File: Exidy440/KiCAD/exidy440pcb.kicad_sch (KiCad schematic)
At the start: 0 parts

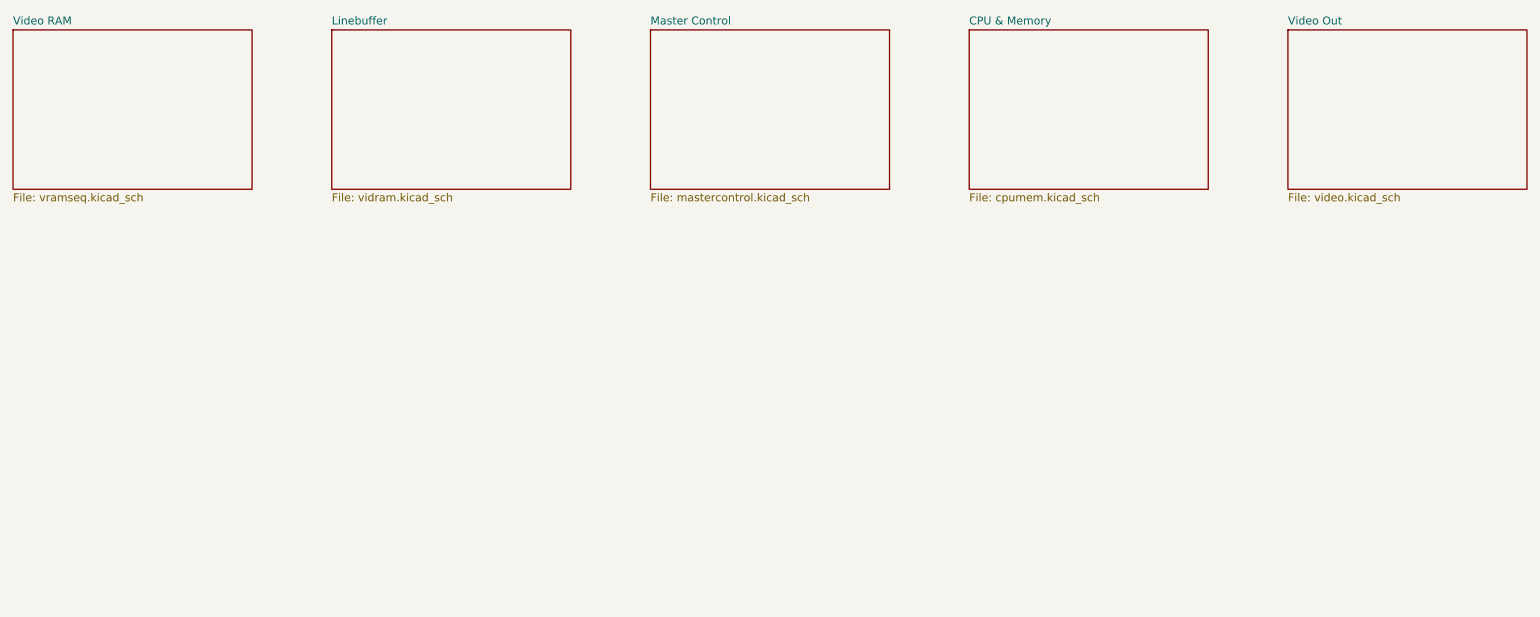
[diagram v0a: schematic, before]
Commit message: Added dual PCB structure, misc fixes and start of audio board IO
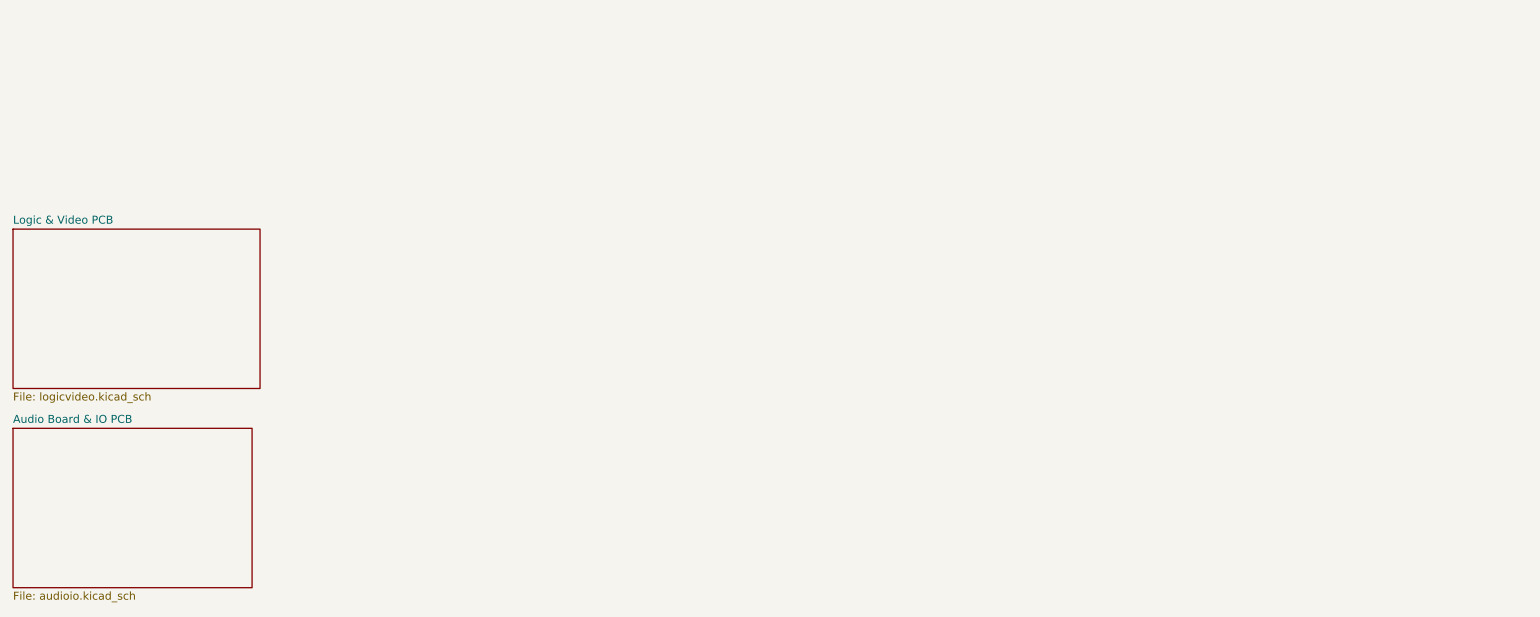
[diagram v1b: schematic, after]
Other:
- removed sheet CPU & Memory
- removed sheet Linebuffer
- removed sheet Master Control
- removed sheet Video Out
- removed sheet Video RAM
- added sheet Audio Board & IO PCB (audioio.kicad_sch)
- added sheet Logic & Video PCB (logicvideo.kicad_sch)
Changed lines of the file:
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@@
 	)
 	(sheet
-		(at 127 25.4)
+		(at 25.4 88.9)
 		(size 38.1 25.4)
 		(fields_autoplaced yes)
@@
 			(color 0 0 0 0.0000)
 		)
-		(property "Sheetname" "Master Control"
-			(at 127 24.6884 0)
+		(property "Sheetname" "Audio Board & IO PCB"
+			(at 25.4 88.1884 0)
 			(effects
 				(font
@@
 			)
 		)
-		(property "Sheetfile" "mastercontrol.kicad_sch"
-			(at 127 51.3846 0)
+		(property "Sheetfile" "audioio.kicad_sch"
+			(at 25.4 114.8846 0)
 			(effects
 				(font
@@
 			(project "exidy440pcb"
 				(path "/ee9ca5df-edb9-4677-bdcd-afd3abb310eb"
-					(page "3")
+					(page "AIDX")
 				)
 			)
@@
 	)
 	(sheet
-		(at 76.2 25.4)
-		(size 38.1 25.4)
+		(at 25.4 57.15)
+		(size 39.37 25.4)
 		(fields_autoplaced yes)
 		(stroke
@@
 			(color 0 0 0 0.0000)
 		)
-		(property "Sheetname" "Linebuffer"
-			(at 76.2 24.6884 0)
+		(property "Sheetname" "Logic & Video PCB"
+			(at 25.4 56.4384 0)
 			(effects
 				(font
@@
 			)
 		)
-		(property "Sheetfile" "vidram.kicad_sch"
-			(at 76.2 51.3846 0)
+		(property "Sheetfile" "logicvideo.kicad_sch"
+			(at 25.4 83.1346 0)
 			(effects
 				(font
@@
 			(project "exidy440pcb"
 				(path "/ee9ca5df-edb9-4677-bdcd-afd3abb310eb"
-					(page "2")
-				)
-			)
-		)
-	)
-	(sheet
-		(at 228.6 25.4)
-		(size 38.1 25.4)
-		(fields_autoplaced yes)
-		(stroke
-			(width 0.1524)
-			(type solid)
-		)
-		(fill
-			(color 0 0 0 0.0000)
-		)
-		(property "Sheetname" "Video Out"
-			(at 228.6 24.6884 0)
-			(effects
-				(font
-					(size 1.27 1.27)
-				)
-				(justify left bottom)
-			)
-		)
-		(property "Sheetfile" "video.kicad_sch"
-			(at 228.6 51.3846 0)
-			(effects
-				(font
-					(size 1.27 1.27)
-				)
-				(justify left top)
-			)
-		)
-		(instances
-			(project "exidy440pcb"
-				(path "/ee9ca5df-edb9-4677-bdcd-afd3abb310eb"
-					(page "5")
-				)
-			)
-		)
-	)
-	(sheet
-		(at 25.4 25.4)
-		(size 38.1 25.4)
-		(fields_autoplaced yes)
-		(stroke
-			(width 0.1524)
-			(type solid)
-		)
-		(fill
-			(color 0 0 0 0.0000)
-		)
-		(property "Sheetname" "Video RAM"
-			(at 25.4 24.6884 0)
-			(effects
-				(font
-					(size 1.27 1.27)
-				)
-				(justify left bottom)
-			)
-		)
-		(property "Sheetfile" "vramseq.kicad_sch"
-			(at 25.4 51.3846 0)
-			(effects
-				(font
-					(size 1.27 1.27)
-				)
-				(justify left top)
-			)
-		)
-		(instances
-			(project "exidy440pcb"
-				(path "/ee9ca5df-edb9-4677-bdcd-afd3abb310eb"
-					(page "1")
-				)
-			)
-		)
-	)
-	(sheet
-		(at 177.8 25.4)
-		(size 38.1 25.4)
-		(fields_autoplaced yes)
-		(stroke
-			(width 0.1524)
-			(type solid)
-		)
-		(fill
-			(color 0 0 0 0.0000)
-		)
-		(property "Sheetname" "CPU & Memory"
-			(at 177.8 24.6884 0)
-			(effects
-				(font
-					(size 1.27 1.27)
-				)
-				(justify left bottom)
-			)
-		)
-		(property "Sheetfile" "cpumem.kicad_sch"
-			(at 177.8 51.3846 0)
-			(effects
-				(font
-					(size 1.27 1.27)
-				)
-				(justify left top)
-			)
-		)
-		(instances
-			(project "exidy440pcb"
-				(path "/ee9ca5df-edb9-4677-bdcd-afd3abb310eb"
-					(page "4")
+					(page "LIDX")
 				)
 			)
@@
 	(sheet_instances
 		(path "/"
-			(page "0")
+			(page "440IDX")
 		)
 	)

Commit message: Minor modifications to IO board
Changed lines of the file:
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@@
 	)
 	(sheet
-		(at 25.4 88.9)
-		(size 38.1 25.4)
+		(at 152.4 25.4)
+		(size 114.3 76.2)
 		(fields_autoplaced yes)
 		(stroke
@@
 		)
 		(property "Sheetname" "Audio Board & IO PCB"
-			(at 25.4 88.1884 0)
+			(at 152.4 24.6884 0)
 			(effects
 				(font
@@
 		)
 		(property "Sheetfile" "audioio.kicad_sch"
-			(at 25.4 114.8846 0)
+			(at 152.4 102.1846 0)
 			(effects
 				(font
@@
 	)
 	(sheet
-		(at 25.4 57.15)
-		(size 39.37 25.4)
+		(at 25.4 25.4)
+		(size 114.3 76.2)
 		(fields_autoplaced yes)
 		(stroke
@@
 		)
 		(property "Sheetname" "Logic & Video PCB"
-			(at 25.4 56.4384 0)
+			(at 25.4 24.6884 0)
 			(effects
 				(font
@@
 		)
 		(property "Sheetfile" "logicvideo.kicad_sch"
-			(at 25.4 83.1346 0)
+			(at 25.4 102.1846 0)
 			(effects
 				(font
